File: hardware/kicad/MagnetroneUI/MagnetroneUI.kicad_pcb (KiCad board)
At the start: 2 copper layers, 120 x 50 mm, 28 parts, among them J1 Conn_01x04, J2 Conn_02x13_Counter_Clockwise, Q1 BSS138, Q2 BSS138, SW1 SW_Push, SW2 RotaryEncoder_Switch_MP, SW3 RotaryEncoder_Switch_MP, SW4 RotaryEncoder_Switch_MP, SW5 RotaryEncoder_Switch_MP, SW6 RotaryEncoder_Switch_MP

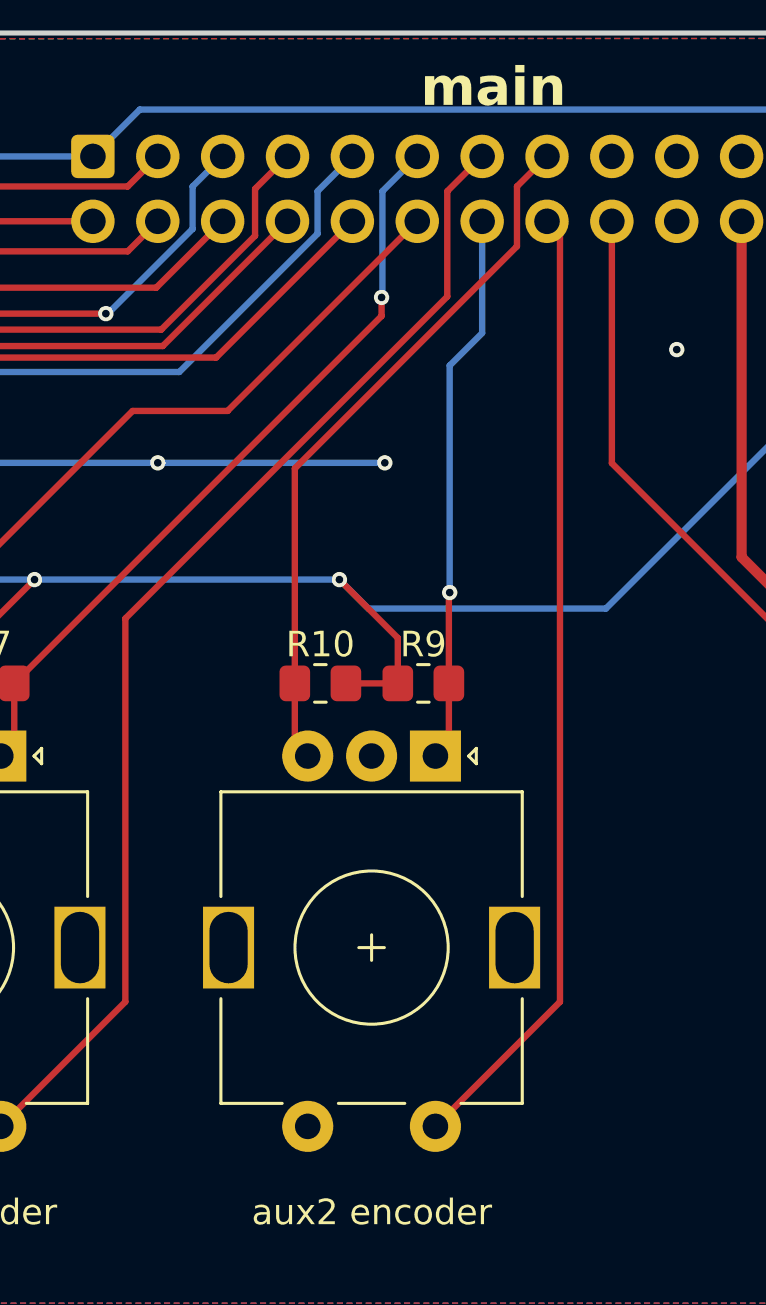
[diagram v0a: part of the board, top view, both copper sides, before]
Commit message: chore: replace motor driver
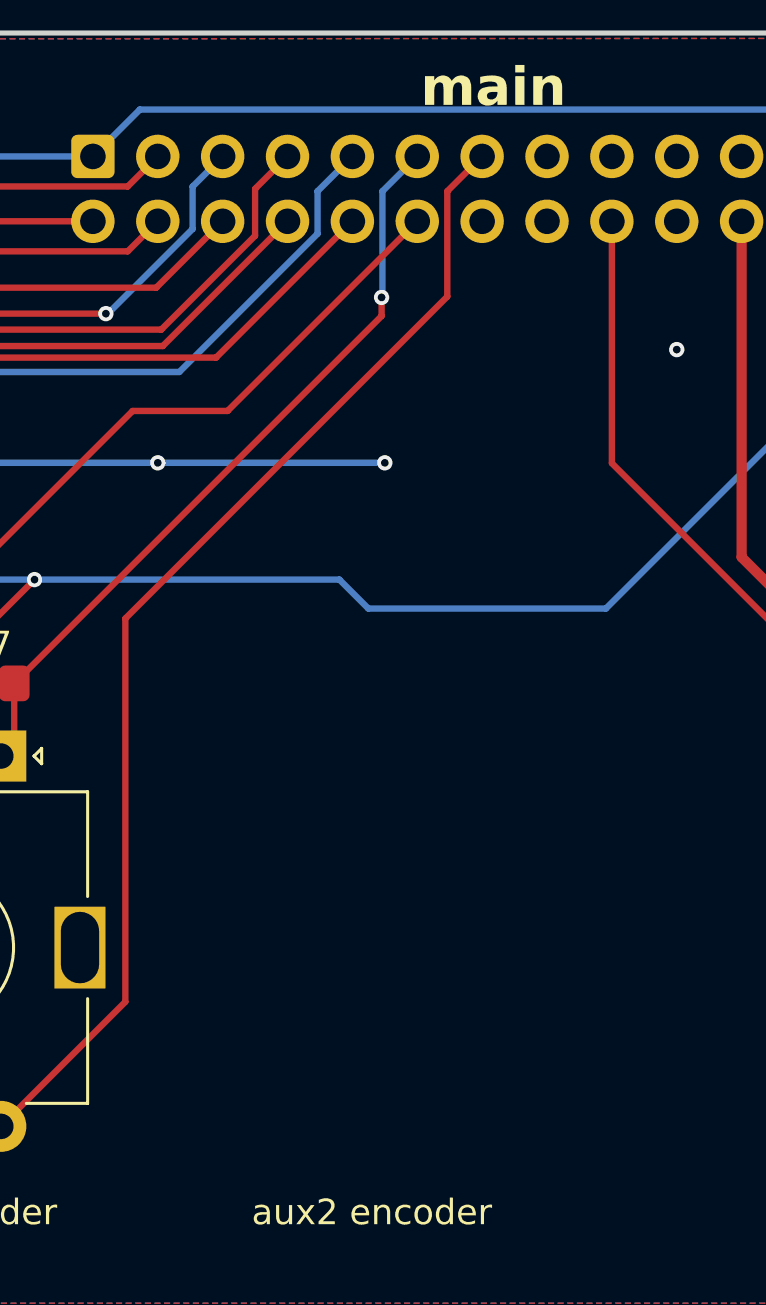
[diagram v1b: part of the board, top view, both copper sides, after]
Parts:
- removed R10, R9: 10k, Resistor_SMD:R_0805_2012Metric_Pad1.20x1.40mm_HandSolder
- removed SW6: RotaryEncoder_Switch_MP, Rotary_Encoder:RotaryEncoder_Alps_EC11E-Switch_Vertical_H20mm
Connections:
- J2 pad 14: /encoder_aux2_a -> unconnected-(J2-Pin_14-Pad14)
- J2 pad 15: /encoder_aux2_b -> unconnected-(J2-Pin_15-Pad15)
- J2 pad 16: /encoder_aux2_btn -> unconnected-(J2-Pin_16-Pad16)
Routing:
- net /encoder_aux2_btn: track 36.9 -> 0.00 mm
- net /encoder_aux2_b: track 27.1 -> 0.00 mm
- net /encoder_aux2_a: track 21.0 -> 0.00 mm, vias 1 -> 0
- net +3.3V: track 264.5 -> 257.4 mm, vias 7 -> 6
